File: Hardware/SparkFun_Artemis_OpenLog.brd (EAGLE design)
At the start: 30.5 x 30.5 mm, 126 parts, among them J14 CORTEX_JTAG, J6 MICRO-SD, Q1 20V/0.2A/8MHz/1.2Ω/1Vth, Q10 20V/0.2A/8MHz/1.2Ω/1Vth, Q2 20V/4.2A/52mΩ/1.4W, Q3 20V/0.2A/8MHz/1.2Ω/1Vth, Q7 20V/0.2A/8MHz/1.2Ω/1Vth, Q9 20V/0.2A/8MHz/1.2Ω/1Vth, U1 3.0V Supervisor, U10 CH340E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

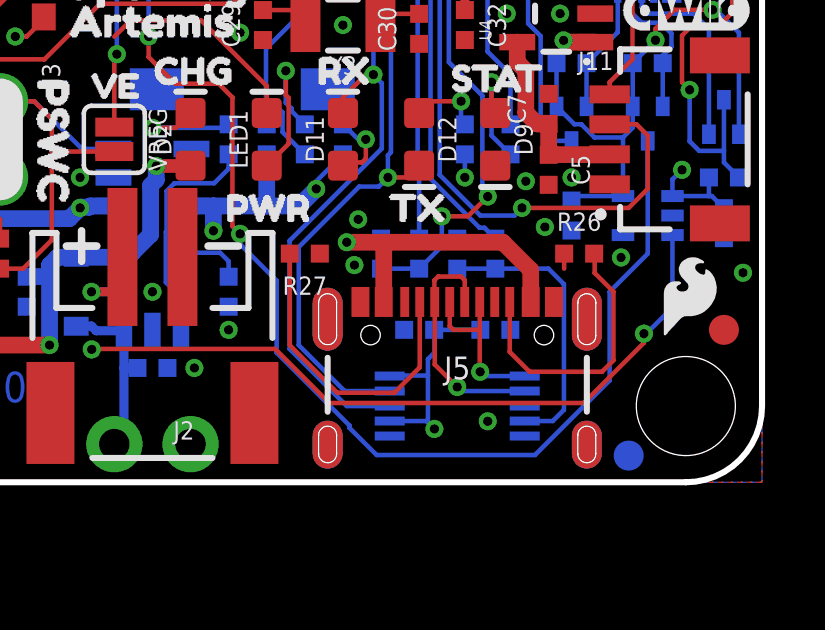
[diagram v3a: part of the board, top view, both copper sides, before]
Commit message: Increase VIN and 5V traces to polygon pours on internal layer.
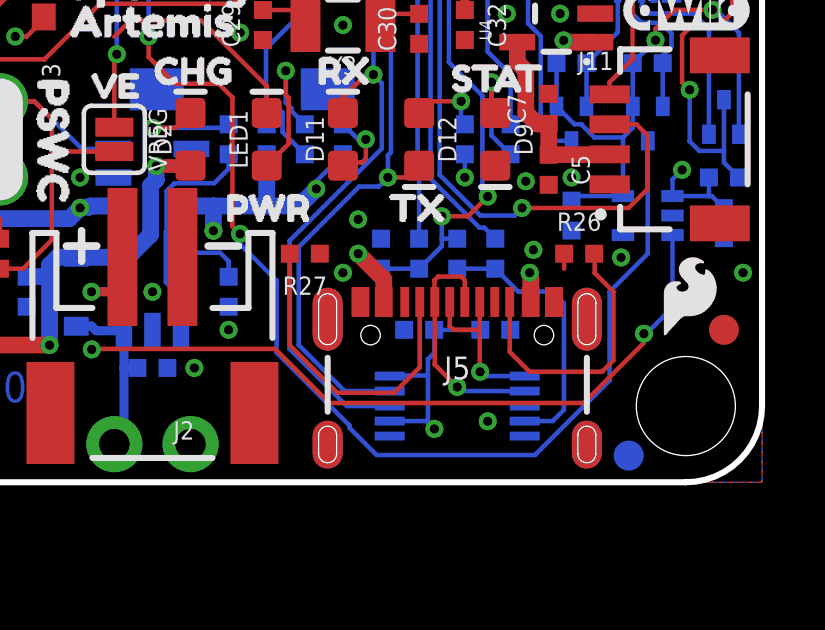
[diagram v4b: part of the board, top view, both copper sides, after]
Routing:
- net 5V: track 39.9 -> 20.7 mm, vias 3 -> 4
- net VIN: track 34.6 -> 16.1 mm
- added copper zone on layer 15, net 5V
- added copper zone on layer 15, net VIN

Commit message: Update SparkFun_Artemis_OpenLog.brd
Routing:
- net VCC_1: track 26.9 -> 33.2 mm, vias 2 -> 4
- net N$1: track 7.88 -> 5.07 mm, vias 2 -> 0
- net 5V: track 20.7 -> 22.5 mm, vias 4 -> 6
- net V_BATT: track 10.3 -> 11.6 mm, vias 1 -> 2
- net VIN: track 16.1 -> 17.0 mm, vias 2 -> 3
- net 3.3V: vias 8 -> 9
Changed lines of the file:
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@@
 <layers>
 <layer number="1" name="Top" color="4" fill="1" visible="yes" active="yes"/>
-<layer number="2" name="Vertical" color="1" fill="3" visible="no" active="yes"/>
-<layer number="15" name="Horz" color="4" fill="6" visible="no" active="yes"/>
+<layer number="2" name="Vertical" color="1" fill="3" visible="yes" active="yes"/>
+<layer number="15" name="Horz" color="4" fill="6" visible="yes" active="yes"/>
 <layer number="16" name="Bottom" color="1" fill="1" visible="yes" active="yes"/>
 <layer number="17" name="Pads" color="2" fill="1" visible="yes" active="yes"/>
@@
 <layer number="19" name="Unrouted" color="6" fill="1" visible="yes" active="yes"/>
 <layer number="20" name="Dimension" color="24" fill="1" visible="yes" active="yes"/>
-<layer number="21" name="tPlace" color="16" fill="1" visible="yes" active="yes"/>
-<layer number="22" name="bPlace" color="14" fill="1" visible="yes" active="yes"/>
-<layer number="23" name="tOrigins" color="15" fill="1" visible="yes" active="yes"/>
-<layer number="24" name="bOrigins" color="15" fill="1" visible="yes" active="yes"/>
+<layer number="21" name="tPlace" color="16" fill="1" visible="no" active="yes"/>
+<layer number="22" name="bPlace" color="14" fill="1" visible="no" active="yes"/>
+<layer number="23" name="tOrigins" color="15" fill="1" visible="no" active="yes"/>
+<layer number="24" name="bOrigins" color="15" fill="1" visible="no" active="yes"/>
 <layer number="25" name="tNames" color="7" fill="1" visible="no" active="yes"/>
 <layer number="26" name="bNames" color="7" fill="1" visible="no" active="yes"/>
@@
 <layer number="43" name="vRestrict" color="2" fill="10" visible="no" active="yes"/>
 <layer number="44" name="Drills" color="7" fill="1" visible="no" active="yes"/>
-<layer number="45" name="Holes" color="7" fill="1" visible="yes" active="yes"/>
+<layer number="45" name="Holes" color="7" fill="1" visible="no" active="yes"/>
 <layer number="46" name="Milling" color="3" fill="1" visible="no" active="yes"/>
 <layer number="47" name="Measures" color="7" fill="1" visible="no" active="yes"/>
 <layer number="48" name="Document" color="7" fill="1" visible="no" active="yes"/>
-<layer number="49" name="Reference" color="7" fill="1" visible="yes" active="yes"/>
+<layer number="49" name="Reference" color="7" fill="1" visible="no" active="yes"/>
 <layer number="50" name="dxf" color="7" fill="1" visible="no" active="yes"/>
-<layer number="51" name="tDocu" color="6" fill="1" visible="yes" active="yes"/>
+<layer number="51" name="tDocu" color="6" fill="1" visible="no" active="yes"/>
 <layer number="52" name="bDocu" color="7" fill="1" visible="no" active="yes"/>
 <layer number="91" name="Nets" color="2" fill="1" visible="no" active="no"/>
@@
 <contactref element="C7" pad="2"/>
 <contactref element="U4" pad="2"/>
-<via x="23.749" y="15.621" extent="1-16" drill="0.3048"/>
+<via x="23.876" y="16.002" extent="1-16" drill="0.3048"/>
 <contactref element="R3" pad="1"/>
 <wire x1="11.43" y1="1.27" x2="-4.31" y2="-29.21" width="0" layer="19" extent="1-1"/>
@@
 <wire x1="23.76838125" y1="18.669" x2="23.5204" y2="18.91698125" width="0.1524" layer="1"/>
 <via x="23.5204" y="18.91698125" extent="1-16" drill="0.3048"/>
+<via x="13.97" y="9.271" extent="1-16" drill="0.3048"/>
 </signal>
 <signal name="VIN" class="1">
@@
 <vertex x="0" y="10.16"/>
 </polygon>
+<via x="23.35554375" y="15.3622" extent="1-16" drill="0.3048"/>
+<wire x1="23.35554375" y1="15.3622" x2="23.35554375" y2="15.2352" width="0.4572" layer="1"/>
+<wire x1="23.35554375" y1="15.2352" x2="23.86354375" y2="14.7272" width="0.4572" layer="1"/>
 </signal>
 <signal name="N$7">
@@
 <wire x1="9.017" y1="6.35" x2="9.16" y2="6.493" width="0.1524" layer="1"/>
 <wire x1="8.89" y1="6.35" x2="8.128" y2="6.35" width="0.3048" layer="16"/>
+<via x="7.493" y="6.35" extent="1-16" drill="0.3048"/>
+<wire x1="7.493" y1="6.35" x2="8.128" y2="6.35" width="0.3048" layer="1"/>
+<wire x1="7.493" y1="6.35" x2="8.128" y2="6.35" width="0.3048" layer="16"/>
 </signal>
 <signal name="ARTEMIS_SWDIO">
@@
 <wire x1="22.77" y1="6.01" x2="22.77" y2="6.948" width="0.5588" layer="1"/>
 <wire x1="22.77" y1="6.948" x2="22.733" y2="6.985" width="0.5588" layer="1"/>
+<via x="5.842" y="4.572" extent="1-16" drill="0.3048"/>
+<wire x1="5.842" y1="4.572" x2="6.731" y2="4.572" width="0.5588" layer="16"/>
+<via x="4.953" y="4.572" extent="1-16" drill="0.3048"/>
+<wire x1="4.953" y1="4.572" x2="5.842" y2="4.572" width="0.5588" layer="16"/>
 </signal>
 <signal name="N$25">
@@
 <wire x1="22.6822" y1="20.3765625" x2="21.6973625" y2="21.3614" width="0.1524" layer="16"/>
 <contactref element="J6" pad="DI"/>
-<wire x1="23.1014" y1="11.8236" x2="23.1014" y2="14.8716" width="0.1524" layer="16"/>
-<wire x1="23.1014" y1="14.8716" x2="22.6822" y2="15.2908" width="0.1524" layer="16"/>
-<wire x1="22.6822" y1="15.2908" x2="22.6822" y2="20.3765625" width="0.1524" layer="16"/>
+<wire x1="23.1014" y1="11.8236" x2="23.1014" y2="14.6176" width="0.1524" layer="16"/>
+<wire x1="23.1014" y1="14.6176" x2="22.6822" y2="15.0368" width="0.1524" layer="16"/>
+<wire x1="22.6822" y1="15.0368" x2="22.6822" y2="20.3765625" width="0.1524" layer="16"/>
 <wire x1="15.494" y1="26.67905625" x2="15.2146" y2="26.95845625" width="0.1524" layer="16"/>
 <wire x1="15.2146" y1="26.95845625" x2="15.2146" y2="27.40034375" width="0.1524" layer="16"/>
@@
 <contactref element="R1" pad="1"/>
 <contactref element="D3" pad="A"/>
-<wire x1="25.026" y1="20.32" x2="25.273" y2="20.32" width="0.1524" layer="1"/>
-<wire x1="25.281" y1="20.312" x2="26.162" y2="20.312" width="0.1524" layer="1"/>
-<wire x1="25.273" y1="20.32" x2="25.281" y2="20.312" width="0.1524" layer="1"/>
-<wire x1="25.026" y1="20.32" x2="24.899" y2="20.447" width="0.1524" layer="1"/>
-<wire x1="24.899" y1="20.447" x2="23.6982" y2="20.447" width="0.1524" layer="1"/>
-<via x="23.6982" y="20.447" extent="1-16" drill="0.3048"/>
-<wire x1="21.727" y1="21.981" x2="21.727" y2="21.844" width="0.1524" layer="1"/>
-<wire x1="21.7932" y1="22.352" x2="20.574" y2="22.352" width="0.1524" layer="16"/>
-<via x="20.574" y="22.352" extent="1-16" drill="0.3048"/>
-<wire x1="20.574" y1="22.352" x2="21.356" y2="22.352" width="0.1524" layer="1"/>
-<wire x1="21.356" y1="22.352" x2="21.727" y2="21.981" width="0.1524" layer="1"/>
-<wire x1="23.6982" y1="20.447" x2="21.7932" y2="22.352" width="0.1524" layer="16"/>
+<wire x1="21.727" y1="21.844" x2="22.99805" y2="21.844" width="0.3048" layer="1"/>
+<wire x1="24.52205" y1="20.32" x2="25.026" y2="20.32" width="0.3048" layer="1"/>
+<wire x1="22.99805" y1="21.844" x2="24.52205" y2="20.32" width="0.3048" layer="1"/>
+<wire x1="26.162" y1="20.312" x2="25.034" y2="20.312" width="0.3048" layer="1"/>
+<wire x1="25.034" y1="20.312" x2="25.026" y2="20.32" width="0.3048" layer="1"/>
 </signal>
 <signal name="VCC_1">
@@
 <wire x1="24.235" y1="19.431" x2="23.8684875" y2="19.431" width="0.3048" layer="1"/>
 <wire x1="23.8684875" y1="19.431" x2="23.77290625" y2="19.52658125" width="0.3048" layer="1"/>
-<wire x1="23.77290625" y1="19.52658125" x2="23.26789375" y2="19.52658125" width="0.3048" layer="1"/>
+<wire x1="23.77290625" y1="19.52658125" x2="23.622" y2="19.52658125" width="0.3048" layer="1"/>
+<wire x1="23.622" y1="19.52658125" x2="23.26789375" y2="19.52658125" width="0.3048" layer="1"/>
 <wire x1="23.26789375" y1="19.52658125" x2="23.1723125" y2="19.431" width="0.3048" layer="1"/>
 <wire x1="23.1723125" y1="19.431" x2="22.726" y2="19.431" width="0.3048" layer="1"/>
@@
 <wire x1="18.99994375" y1="17.98394375" x2="19.177" y2="18.161" width="0.1524" layer="16"/>
 <wire x1="18.99994375" y1="10.36394375" x2="18.99994375" y2="17.98394375" width="0.1524" layer="16"/>
-<wire x1="24.0795125" y1="19.65358125" x2="23.2152875" y2="19.65358125" width="0.5588" layer="15"/>
+<wire x1="24.0795125" y1="19.65358125" x2="23.622" y2="19.65358125" width="0.5588" layer="15"/>
+<wire x1="23.622" y1="19.65358125" x2="23.2152875" y2="19.65358125" width="0.5588" layer="15"/>
 <wire x1="24.235" y1="19.431" x2="24.235" y2="19.49809375" width="0.5588" layer="15"/>
 <wire x1="24.235" y1="19.49809375" x2="24.0795125" y2="19.65358125" width="0.5588" layer="15"/>
 <wire x1="21.72270625" y1="18.161" x2="19.177" y2="18.161" width="0.5588" layer="15"/>
 <wire x1="23.2152875" y1="19.65358125" x2="21.72270625" y2="18.161" width="0.5588" layer="15"/>
+<via x="23.6" y="20.066" extent="1-16" drill="0.3048"/>
+<wire x1="23.6" y1="20.066" x2="23.6" y2="19.54858125" width="0.3048" layer="1"/>
+<wire x1="23.6" y1="19.54858125" x2="23.622" y2="19.52658125" width="0.3048" layer="1"/>
+<wire x1="23.6" y1="20.066" x2="23.6" y2="19.67558125" width="0.5588" layer="15"/>
+<wire x1="23.6" y1="19.67558125" x2="23.622" y2="19.65358125" width="0.3048" layer="15"/>
+<via x="17.526" y="21.082" extent="1-16" drill="0.3048"/>
+<wire x1="17.526" y1="21.082" x2="17.526" y2="19.812" width="0.5588" layer="15"/>
+<wire x1="17.526" y1="19.812" x2="19.177" y2="18.161" width="0.5588" layer="15"/>
+<wire x1="17.526" y1="21.082" x2="18.24" y2="20.368" width="0.3048" layer="1"/>
+<wire x1="18.24" y1="20.368" x2="18.24" y2="19.7" width="0.3048" layer="1"/>
 </signal>
 <signal name="!POWER_LOSS!">

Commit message: Update SparkFun_Artemis_OpenLog.brd
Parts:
- moved R3 54.3 mm to (21.5, 18.8), turned to 90 degrees
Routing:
- net GND: track 11.9 -> 13.1 mm
- net QWIIC_PWR: track 8.31 -> 8.97 mm
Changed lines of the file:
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@@
 <layer number="19" name="Unrouted" color="6" fill="1" visible="yes" active="yes"/>
 <layer number="20" name="Dimension" color="24" fill="1" visible="yes" active="yes"/>
-<layer number="21" name="tPlace" color="16" fill="1" visible="no" active="yes"/>
-<layer number="22" name="bPlace" color="14" fill="1" visible="no" active="yes"/>
-<layer number="23" name="tOrigins" color="15" fill="1" visible="no" active="yes"/>
-<layer number="24" name="bOrigins" color="15" fill="1" visible="no" active="yes"/>
+<layer number="21" name="tPlace" color="16" fill="1" visible="yes" active="yes"/>
+<layer number="22" name="bPlace" color="14" fill="1" visible="yes" active="yes"/>
+<layer number="23" name="tOrigins" color="15" fill="1" visible="yes" active="yes"/>
+<layer number="24" name="bOrigins" color="15" fill="1" visible="yes" active="yes"/>
 <layer number="25" name="tNames" color="7" fill="1" visible="no" active="yes"/>
 <layer number="26" name="bNames" color="7" fill="1" visible="no" active="yes"/>
@@
 <element name="LOGO1" library="SparkFun-Aesthetics" package="SFE_LOGO_NAME_.1" value="SFE_LOGO_NAME.1_INCH" x="15.24" y="28.829" smashed="yes" rot="MR0"/>
 <element name="LOGO5" library="SparkFun-Aesthetics" package="SFE_LOGO_FLAME_.1" value="SFE_LOGO_FLAME.1_INCH" x="15.113" y="3.556" smashed="yes" rot="MR0"/>
-<element name="R3" library="SparkFun-Resistors" package="0402-TIGHT" value="220k" x="-3.81" y="-29.21" smashed="yes">
-<attribute name="NAME" x="-3.81" y="-28.648" size="0.6096" layer="25" font="vector" ratio="20" align="bottom-center"/>
-<attribute name="PROD_ID" value="RES-15094" x="-3.81" y="-29.21" size="1.778" layer="27" font="vector" ratio="15" display="off"/>
-<attribute name="VALUE" x="-3.81" y="-29.772" size="0.6096" layer="27" font="vector" ratio="20" align="top-center"/>
+<element name="R3" library="SparkFun-Resistors" package="0402-TIGHT" value="220k" x="21.463" y="18.796" smashed="yes" rot="R90">
+<attribute name="NAME" x="20.901" y="18.796" size="0.6096" layer="25" font="vector" ratio="20" rot="R90" align="bottom-center"/>
+<attribute name="PROD_ID" value="RES-15094" x="21.463" y="18.796" size="1.778" layer="27" font="vector" ratio="15" rot="R90" display="off"/>
+<attribute name="VALUE" x="22.025" y="18.796" size="0.6096" layer="27" font="vector" ratio="20" rot="R90" align="top-center"/>
 </element>
 </elements>
@@
 <via x="23.876" y="16.002" extent="1-16" drill="0.3048"/>
 <contactref element="R3" pad="1"/>
-<wire x1="11.43" y1="1.27" x2="-4.31" y2="-29.21" width="0" layer="19" extent="1-1"/>
+<wire x1="24.9221" y1="15.621" x2="24.257" y2="15.621" width="0.4572" layer="1"/>
+<wire x1="24.257" y1="15.621" x2="23.876" y2="16.002" width="0.4572" layer="1"/>
 </signal>
 <signal name="3.3V">
@@
 <contactref element="U8" pad="~D18"/>
 <wire x1="19.74" y1="20.9" x2="21.505" y2="20.9" width="0.1524" layer="1"/>
-<wire x1="21.505" y1="20.9" x2="21.86405625" y2="20.54094375" width="0.1524" layer="1"/>
+<wire x1="21.505" y1="20.9" x2="22.11805625" y2="20.28694375" width="0.1524" layer="1"/>
 <contactref element="U4" pad="3"/>
-<wire x1="21.86405625" y1="18.26794375" x2="21.86405625" y2="20.54094375" width="0.1524" layer="1"/>
+<wire x1="22.11805625" y1="18.01394375" x2="22.11805625" y2="19.304" width="0.1524" layer="1"/>
+<wire x1="22.11805625" y1="19.304" x2="22.11805625" y2="20.28694375" width="0.1524" layer="1"/>
 <wire x1="24.9221" y1="16.571" x2="23.561" y2="16.571" width="0.1524" layer="1"/>
-<wire x1="23.561" y1="16.571" x2="21.86405625" y2="18.26794375" width="0.1524" layer="1"/>
+<wire x1="23.561" y1="16.571" x2="22.11805625" y2="18.01394375" width="0.1524" layer="1"/>
 <contactref element="R3" pad="2"/>
-<wire x1="-3.31" y1="-29.21" x2="24.9221" y2="16.571" width="0" layer="19" extent="1-1"/>
+<wire x1="21.463" y1="19.296" x2="22.11005625" y2="19.296" width="0.1524" layer="1"/>
+<wire x1="22.11005625" y1="19.296" x2="22.11805625" y2="19.304" width="0.1524" layer="1"/>
 </signal>
 <signal name="SD_PWR">

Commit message: Update SparkFun_Artemis_OpenLog.brd
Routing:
- net GND: track 13.1 -> 17.7 mm
- net ARTEMIS_RX0: track 38.6 -> 37.8 mm, vias 3 -> 2
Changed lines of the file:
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@@
 <layer number="37" name="tTest" color="7" fill="1" visible="no" active="yes"/>
 <layer number="38" name="bTest" color="7" fill="1" visible="no" active="yes"/>
-<layer number="39" name="tKeepout" color="4" fill="11" visible="no" active="yes"/>
+<layer number="39" name="tKeepout" color="4" fill="11" visible="yes" active="yes"/>
 <layer number="40" name="bKeepout" color="1" fill="11" visible="no" active="yes"/>
 <layer number="41" name="tRestrict" color="4" fill="10" visible="no" active="yes"/>
@@
 <element name="LOGO1" library="SparkFun-Aesthetics" package="SFE_LOGO_NAME_.1" value="SFE_LOGO_NAME.1_INCH" x="15.24" y="28.829" smashed="yes" rot="MR0"/>
 <element name="LOGO5" library="SparkFun-Aesthetics" package="SFE_LOGO_FLAME_.1" value="SFE_LOGO_FLAME.1_INCH" x="15.113" y="3.556" smashed="yes" rot="MR0"/>
-<element name="R3" library="SparkFun-Resistors" package="0402-TIGHT" value="220k" x="21.463" y="18.796" smashed="yes" rot="R90">
-<attribute name="NAME" x="20.901" y="18.796" size="0.6096" layer="25" font="vector" ratio="20" rot="R90" align="bottom-center"/>
-<attribute name="PROD_ID" value="RES-15094" x="21.463" y="18.796" size="1.778" layer="27" font="vector" ratio="15" rot="R90" display="off"/>
-<attribute name="VALUE" x="22.025" y="18.796" size="0.6096" layer="27" font="vector" ratio="20" rot="R90" align="top-center"/>
+<element name="R3" library="SparkFun-Resistors" package="0402-TIGHT" value="220k" x="21.463" y="18.8214" smashed="yes" rot="R90">
+<attribute name="NAME" x="20.901" y="18.8214" size="0.6096" layer="25" font="vector" ratio="20" rot="R90" align="bottom-center"/>
+<attribute name="PROD_ID" value="RES-15094" x="21.463" y="18.8214" size="1.778" layer="27" font="vector" ratio="15" rot="R90" display="off"/>
+<attribute name="VALUE" x="22.025" y="18.8214" size="0.6096" layer="27" font="vector" ratio="20" rot="R90" align="top-center"/>
 </element>
 </elements>
@@
 <wire x1="28.2385" y1="16.764" x2="28.956" y2="16.764" width="0.1524" layer="16"/>
 <via x="28.956" y="16.764" extent="1-16" drill="0.3048"/>
-<wire x1="23.884" y1="7.12" x2="23.884" y2="7.62" width="0.1524" layer="1"/>
 <contactref element="J4" pad="6"/>
 <via x="3.302" y="12.446" extent="1-16" drill="0.3048"/>
@@
 <wire x1="24.9221" y1="15.621" x2="24.257" y2="15.621" width="0.4572" layer="1"/>
 <wire x1="24.257" y1="15.621" x2="23.876" y2="16.002" width="0.4572" layer="1"/>
+<wire x1="23.368" y1="12.946" x2="24.265" y2="13.843" width="0.2032" layer="1"/>
+<wire x1="25.4" y1="13.843" x2="25.781" y2="14.224" width="0.2032" layer="1"/>
+<wire x1="25.781" y1="15.494" x2="25.654" y2="15.621" width="0.2032" layer="1"/>
+<wire x1="25.654" y1="15.621" x2="24.9221" y2="15.621" width="0.2032" layer="1"/>
+<wire x1="24.265" y1="13.843" x2="25.4" y2="13.843" width="0.2032" layer="1"/>
+<wire x1="25.781" y1="14.224" x2="25.781" y2="15.494" width="0.2032" layer="1"/>
 </signal>
 <signal name="3.3V">
@@
 <contactref element="D11" pad="C"/>
 <contactref element="U10" pad="8"/>
-<via x="17.399" y="27.686" extent="1-16" drill="0.3048"/>
 <wire x1="17.526" y1="13.589" x2="17.272" y2="13.589" width="0.1524" layer="1"/>
 <wire x1="16.51" y1="12.827" x2="16.51" y2="12.307" width="0.1524" layer="1"/>
@@
 <wire x1="10.74" y1="28.9" x2="11.867" y2="28.9" width="0.1524" layer="1"/>
 <wire x1="11.867" y1="28.9" x2="12.827" y2="27.94" width="0.1524" layer="1"/>
-<wire x1="12.827" y1="27.94" x2="17.145" y2="27.94" width="0.1524" layer="1"/>
-<wire x1="17.145" y1="27.94" x2="17.399" y2="27.686" width="0.1524" layer="1"/>
+<wire x1="12.827" y1="27.94" x2="15.875" y2="27.94" width="0.1524" layer="1"/>
+<wire x1="15.875" y1="27.94" x2="17.399" y2="26.416" width="0.1524" layer="1"/>
 <wire x1="17.8054" y1="11.12445625" x2="14.732" y2="8.05105625" width="0.1524" layer="16"/>
 <wire x1="17.526" y1="13.589" x2="17.526" y2="13.58134375" width="0.1524" layer="16"/>
@@
 <via x="17.1753" y="24.9223" extent="1-16" drill="0.3048"/>
 <wire x1="17.1753" y1="24.9223" x2="17.399" y2="25.146" width="0.1524" layer="1"/>
-<wire x1="17.399" y1="25.146" x2="17.399" y2="27.686" width="0.1524" layer="1"/>
+<wire x1="17.399" y1="25.146" x2="17.399" y2="26.416" width="0.1524" layer="1"/>
 <wire x1="18.1356" y1="24.003" x2="17.2163" y2="24.9223" width="0.1524" layer="16"/>
 <wire x1="17.526" y1="16.002" x2="18.1864" y2="16.6624" width="0.1524" layer="16"/>
@@
 <wire x1="23.561" y1="16.571" x2="22.11805625" y2="18.01394375" width="0.1524" layer="1"/>
 <contactref element="R3" pad="2"/>
-<wire x1="21.463" y1="19.296" x2="22.11005625" y2="19.296" width="0.1524" layer="1"/>
-<wire x1="22.11005625" y1="19.296" x2="22.11805625" y2="19.304" width="0.1524" layer="1"/>
+<wire x1="21.463" y1="19.3214" x2="22.10065625" y2="19.3214" width="0.1524" layer="1"/>
+<wire x1="22.10065625" y1="19.3214" x2="22.11805625" y2="19.304" width="0.1524" layer="1"/>
 </signal>
 <signal name="SD_PWR">

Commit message: Update SparkFun_Artemis_OpenLog.brd
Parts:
- moved Q10 0.51 mm to (24.9, 22.9)
- moved C51 0.25 mm to (26.4, 22.9)
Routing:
- net ICM-20948-LV_#_1.8V: track 41.0 -> 42.2 mm
